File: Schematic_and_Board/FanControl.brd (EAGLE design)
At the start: 99.1 x 78.7 mm, 45 parts, among them J1 POWER_JACKSLT, Q1 VP3203, Q2 VP3203, T1 2N3904, T2 2N3904, U1 ARDUINO_MINI, U2 LCD-16X2SILK

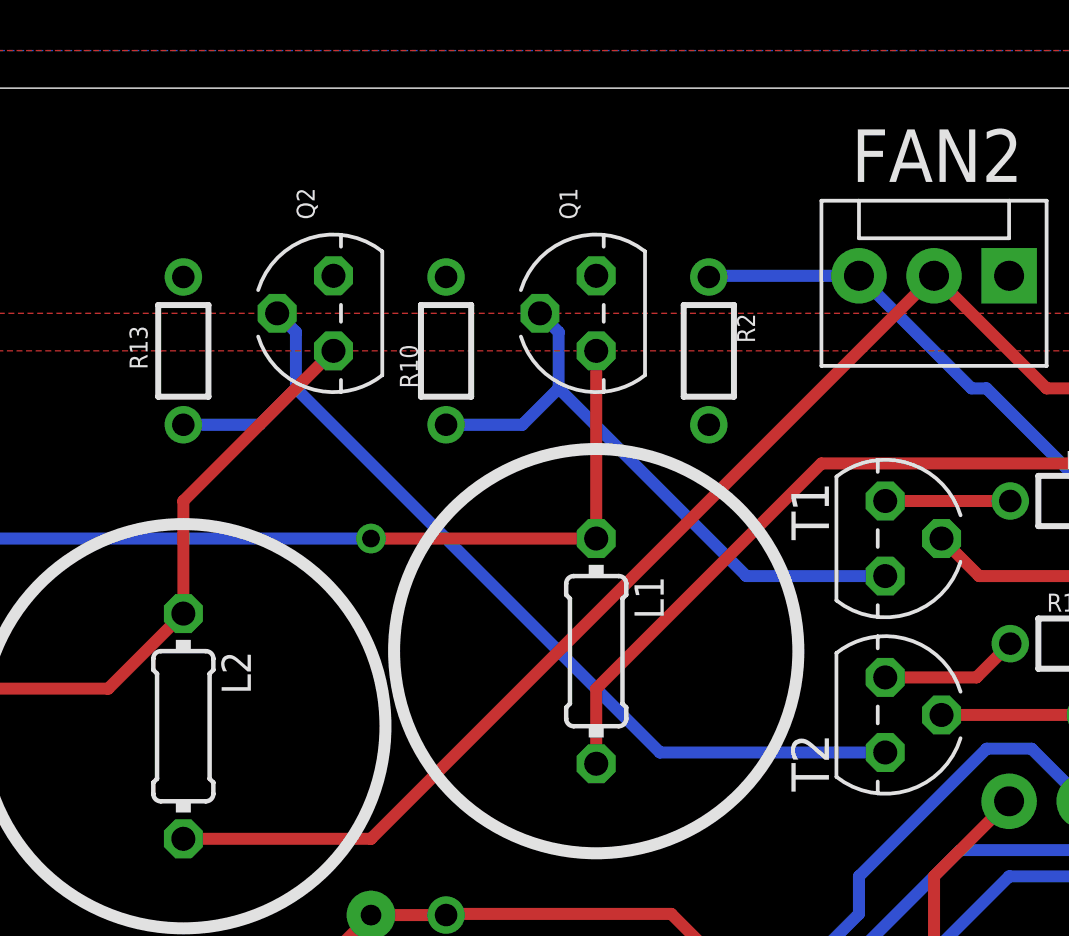
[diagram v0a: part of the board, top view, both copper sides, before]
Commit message: Update Schematic and Board to correct these two errors:
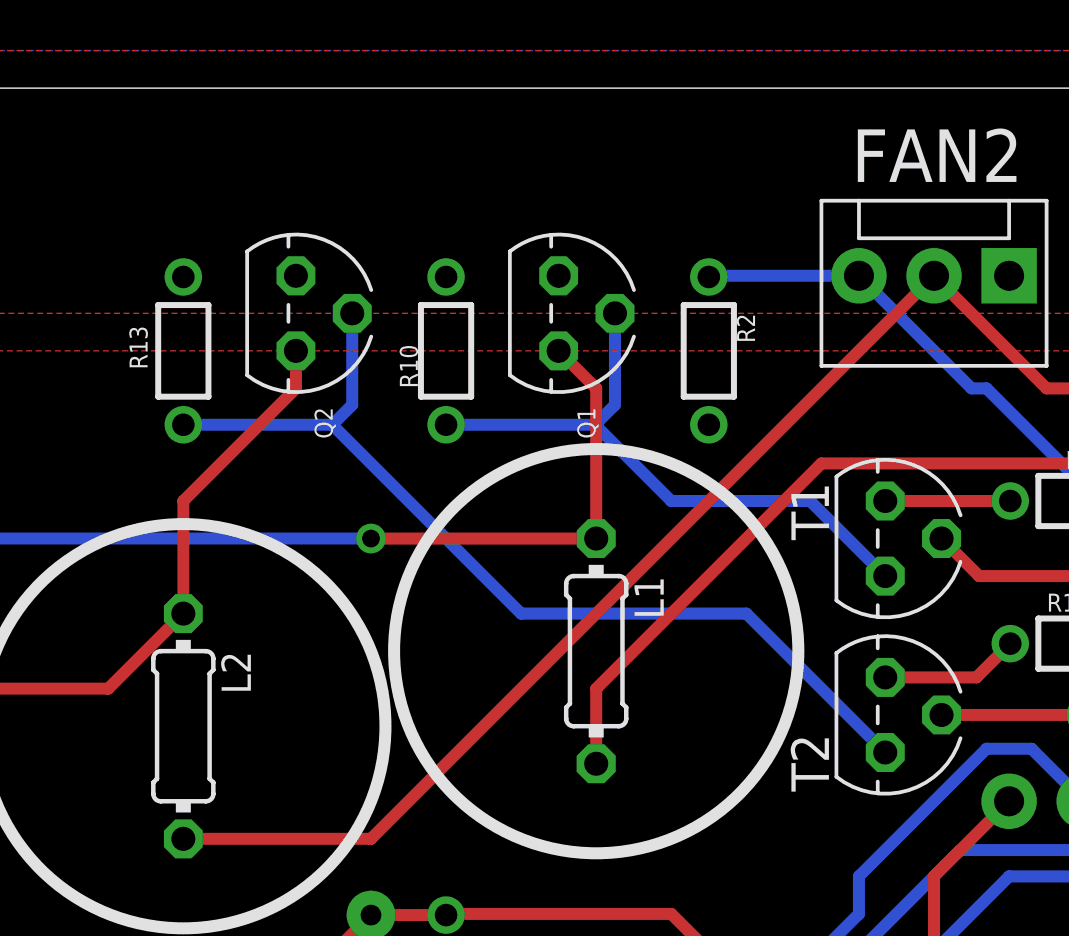
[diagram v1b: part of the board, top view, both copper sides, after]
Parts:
- moved Q1 1.27 mm to (34.3, 71.1), turned to 270 degrees
- moved Q2 1.27 mm to (25.4, 71.1), turned to 270 degrees
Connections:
- net GND: now also J1.GND@1
- net N$11: now also Q1.3; no longer Q1.1
- net N$15: now also Q2.3; no longer Q2.1
- net V12: now also Q1.1, Q2.1; no longer Q1.3, Q2.3
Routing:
- net N$15: track 20.9 -> 20.4 mm
- net N$11: track 29.7 -> 30.3 mm
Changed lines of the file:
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@@
 <attribute name="NAME" x="96.012" y="54.737" size="1.27" layer="25" ratio="10" rot="R180"/>
 </element>
-<element name="Q2" library="transistor-fet" package="TO-92" value="VP3203" x="26.67" y="71.12" smashed="yes" rot="R90">
-<attribute name="NAME" x="26.035" y="74.295" size="0.6096" layer="25" ratio="10" rot="R90"/>
-</element>
-<element name="Q1" library="transistor-fet" package="TO-92" value="VP3203" x="35.56" y="71.12" smashed="yes" rot="R90">
-<attribute name="NAME" x="34.925" y="74.295" size="0.6096" layer="25" ratio="10" rot="R90"/>
+<element name="Q2" library="transistor-fet" package="TO-92" value="VP3203" x="25.4" y="71.12" smashed="yes" rot="R270">
+<attribute name="NAME" x="26.035" y="67.945" size="0.6096" layer="25" ratio="10" rot="R270"/>
+</element>
+<element name="Q1" library="transistor-fet" package="TO-92" value="VP3203" x="34.29" y="71.12" smashed="yes" rot="R270">
+<attribute name="NAME" x="34.925" y="67.945" size="0.6096" layer="25" ratio="10" rot="R270"/>
 </element>
 <element name="R1" library="SparkFun-Passives" package="1/6W-RES" value="10k" x="68.58" y="60.96" smashed="yes">
@@
 <contactref element="U$1" pad="VIN"/>
 <contactref element="R10" pad="2"/>
-<contactref element="Q1" pad="3"/>
 <contactref element="R13" pad="2"/>
-<contactref element="Q2" pad="3"/>
 <polygon width="0.4064" layer="1">
 <vertex x="72.39" y="80.01"/>
@@
 <vertex x="-1.27" y="80.01"/>
 </polygon>
+<contactref element="Q1" pad="1"/>
+<contactref element="Q2" pad="1"/>
 </signal>
 <signal name="GND">
@@
 <wire x1="38.1" y1="41.95" x2="40.64" y2="41.95" width="0.4064" layer="1"/>
 <wire x1="40.64" y1="41.95" x2="43.18" y2="39.41" width="0.4064" layer="1"/>
+<contactref element="J1" pad="GND@1"/>
 </signal>
 <signal name="HALL1">
@@
 <contactref element="T1" pad="1"/>
 <contactref element="Q1" pad="2"/>
-<wire x1="45.339" y1="62.23" x2="40.64" y2="62.23" width="0.4064" layer="16"/>
-<wire x1="40.64" y1="62.23" x2="34.29" y2="68.58" width="0.4064" layer="16"/>
-<wire x1="34.29" y1="68.58" x2="34.29" y2="70.485" width="0.4064" layer="16"/>
-<wire x1="34.29" y1="70.485" x2="33.655" y2="71.12" width="0.4064" layer="16"/>
-<wire x1="30.48" y1="67.35" x2="33.06" y2="67.35" width="0.4064" layer="16"/>
-<wire x1="33.06" y1="67.35" x2="34.29" y2="68.58" width="0.4064" layer="16"/>
+<wire x1="30.48" y1="67.35" x2="35.52" y2="67.35" width="0.4064" layer="16"/>
+<wire x1="35.52" y1="67.35" x2="38.1" y2="64.77" width="0.4064" layer="16"/>
+<wire x1="38.1" y1="64.77" x2="42.799" y2="64.77" width="0.4064" layer="16"/>
+<wire x1="42.799" y1="64.77" x2="45.339" y2="62.23" width="0.4064" layer="16"/>
+<wire x1="36.195" y1="71.12" x2="36.195" y2="68.025" width="0.4064" layer="16"/>
+<wire x1="36.195" y1="68.025" x2="35.52" y2="67.35" width="0.4064" layer="16"/>
 </signal>
 <signal name="N$10">
@@
 </signal>
 <signal name="N$11">
-<contactref element="Q1" pad="1"/>
 <contactref element="D1" pad="C"/>
 <contactref element="L1" pad="1"/>
-<wire x1="35.56" y1="63.5" x2="35.56" y2="69.85" width="0.4064" layer="1"/>
 <wire x1="35.56" y1="63.5" x2="27.94" y2="63.5" width="0.4064" layer="1"/>
 <via x="27.94" y="63.5" extent="1-16" drill="0.6" shape="square"/>
 <wire x1="27.94" y1="63.5" x2="13.97" y2="63.5" width="0.4064" layer="16"/>
 <wire x1="13.97" y1="63.5" x2="12.7" y2="62.23" width="0.4064" layer="16"/>
+<contactref element="Q1" pad="3"/>
+<wire x1="35.56" y1="63.5" x2="35.56" y2="68.58" width="0.4064" layer="1"/>
+<wire x1="35.56" y1="68.58" x2="34.29" y2="69.85" width="0.4064" layer="1"/>
 </signal>
 <signal name="N$12">
@@
 <contactref element="T2" pad="1"/>
 <contactref element="Q2" pad="2"/>
-<wire x1="45.339" y1="56.261" x2="37.719" y2="56.261" width="0.4064" layer="16"/>
-<wire x1="37.719" y1="56.261" x2="25.4" y2="68.58" width="0.4064" layer="16"/>
-<wire x1="25.4" y1="68.58" x2="25.4" y2="70.485" width="0.4064" layer="16"/>
-<wire x1="25.4" y1="70.485" x2="24.765" y2="71.12" width="0.4064" layer="16"/>
-<wire x1="21.59" y1="67.35" x2="24.17" y2="67.35" width="0.4064" layer="16"/>
-<wire x1="24.17" y1="67.35" x2="25.4" y2="68.58" width="0.4064" layer="16"/>
+<wire x1="21.59" y1="67.35" x2="26.63" y2="67.35" width="0.4064" layer="16"/>
+<wire x1="26.63" y1="67.35" x2="33.02" y2="60.96" width="0.4064" layer="16"/>
+<wire x1="33.02" y1="60.96" x2="40.64" y2="60.96" width="0.4064" layer="16"/>
+<wire x1="40.64" y1="60.96" x2="45.339" y2="56.261" width="0.4064" layer="16"/>
+<wire x1="27.305" y1="71.12" x2="27.305" y2="68.025" width="0.4064" layer="16"/>
+<wire x1="27.305" y1="68.025" x2="26.63" y2="67.35" width="0.4064" layer="16"/>
 </signal>
 <signal name="N$13">
@@
 </signal>
 <signal name="N$15">
-<contactref element="Q2" pad="1"/>
 <contactref element="D2" pad="C"/>
 <contactref element="L2" pad="1"/>
 <wire x1="21.59" y1="60.96" x2="21.59" y2="64.77" width="0.4064" layer="1"/>
-<wire x1="21.59" y1="64.77" x2="26.67" y2="69.85" width="0.4064" layer="1"/>
 <wire x1="12.7" y1="58.42" x2="19.05" y2="58.42" width="0.4064" layer="1"/>
 <wire x1="19.05" y1="58.42" x2="21.59" y2="60.96" width="0.4064" layer="1"/>
+<contactref element="Q2" pad="3"/>
+<wire x1="21.59" y1="64.77" x2="25.4" y2="68.58" width="0.4064" layer="1"/>
+<wire x1="25.4" y1="68.58" x2="25.4" y2="69.85" width="0.4064" layer="1"/>
 </signal>
 </signals>
